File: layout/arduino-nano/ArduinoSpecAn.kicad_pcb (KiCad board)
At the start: 4 copper layers, 40.9 x 50.8 mm, 45 parts, among them J1 SMA, J2 SMA, P1 CONN_01X08, P2 CONN_01X06, P3 CONN_01X08, Q1 MMBT3904, Q2 MMBT3904, U1 AD8307, U2 AD9851, U3 LM7301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

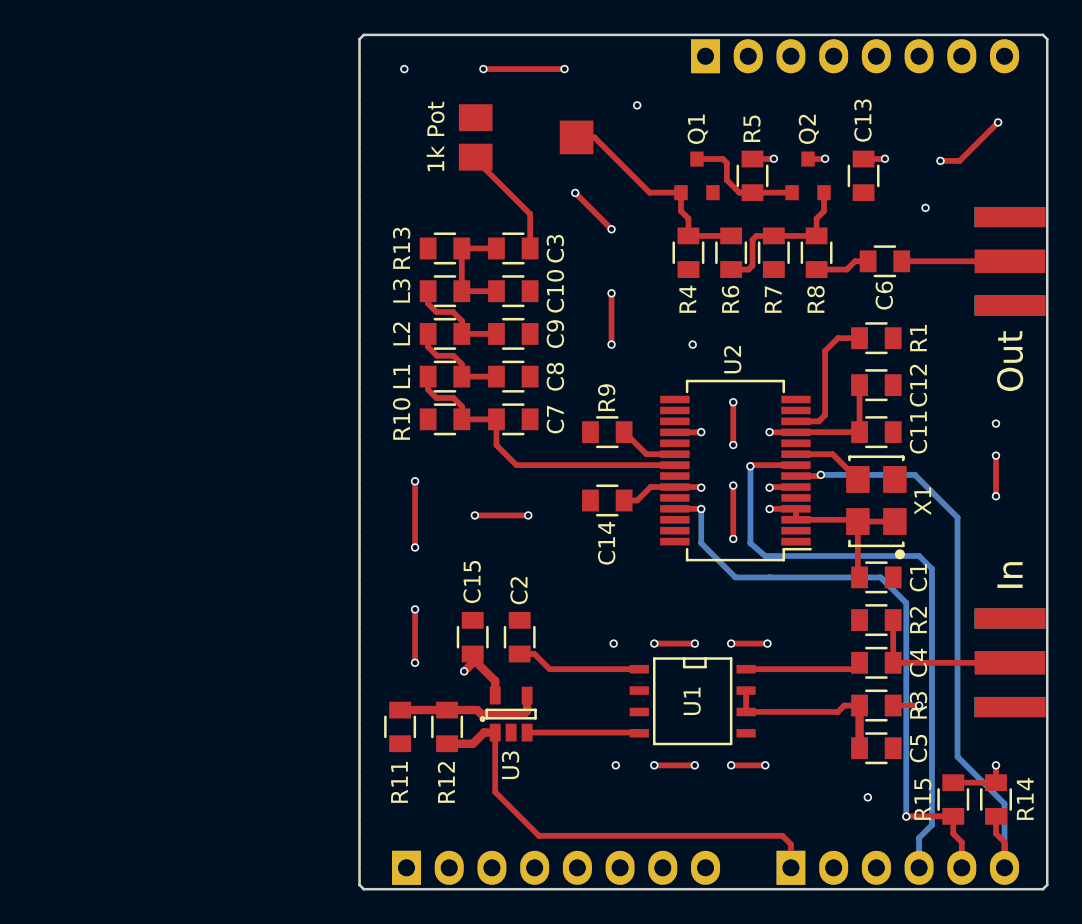
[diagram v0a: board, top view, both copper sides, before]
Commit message: Removed DDS
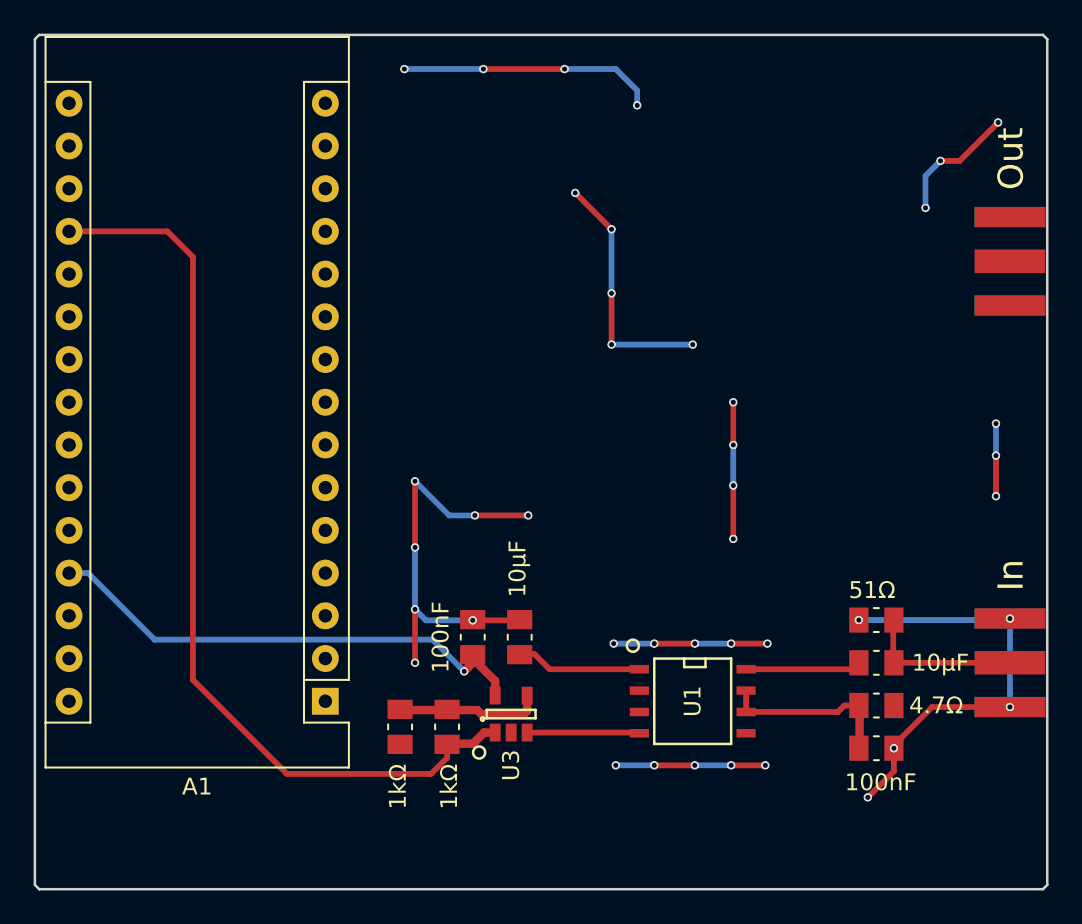
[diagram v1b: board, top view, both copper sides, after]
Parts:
- removed 1k Pot: POT, footprints:ST4ETB_Trim_Pot
- removed C1: .01uF, footprints:Custom_0805
- removed C10, C7: 10pF, footprints:Custom_0805
- removed C11, C12, C13, C14: .1uF, footprints:Custom_0805
- removed C3, C6: 10uF, footprints:Custom_0805
- removed C8, C9: 39pF, footprints:Custom_0805
- removed L1, L3: 270nH, footprints:Custom_0805
- removed L2: 470nH, footprints:Custom_0805
- removed P1, P3: CONN_01X08, Pin_Headers:Pin_Header_Straight_1x08
- removed P2: CONN_01X06, Pin_Headers:Pin_Header_Straight_1x06
- removed Q1, Q2: MMBT3904, footprints:SOT-23
- removed R1: 3k92, footprints:Custom_0805
- removed R10, R13, R4: 100, footprints:Custom_0805
- removed R14, R15: 2k, footprints:Custom_0805
- removed R5, R6, R7: 220, footprints:Custom_0805
- removed R8: 47, footprints:Custom_0805
- removed R9: 50, footprints:Custom_0805
- removed U2: AD9851, Housings_SSOP:SSOP-28_5.3x10.2mm_Pitch0.65mm
- removed X1: KC5032A, footprints:KC5032A-CM_SMD_Crystal
- added A1: Arduino_Nano_v3.x, Module:Arduino_Nano, F.Cu at (125.0, 125.5)
- C15, C5: value .1uF -> 100nF; footprint footprints:Custom_0805 -> Capacitor_SMD:C_0805_2012Metric_Pad1.15x1.50mm_HandSolder
- C2, C4: value 10uF -> 10µF; footprint footprints:Custom_0805 -> Capacitor_SMD:C_0805_2012Metric_Pad1.15x1.50mm_HandSolder
- R11, R12: value 1k -> 1kΩ; footprint footprints:Custom_0805 -> Resistor_SMD:R_0805_2012Metric_Pad1.15x1.50mm_HandSolder
- R2: value 51 -> 51Ω; footprint footprints:Custom_0805 -> Resistor_SMD:R_0805_2012Metric_Pad1.15x1.50mm_HandSolder
- R3: value 4R7 -> 4.7Ω; footprint footprints:Custom_0805 -> Resistor_SMD:R_0805_2012Metric_Pad1.15x1.50mm_HandSolder
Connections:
- net /5V renamed +5V
- J2 pad 1: Net-(C6-Pad2) -> (no net)
- U1 pad 3: Net-(U1-Pad3) -> (no net)
- U1 pad 5: Net-(U1-Pad5) -> (no net)
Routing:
- net /SLD: track 36.8 -> 0.00 mm, vias 1 -> 0
- net /A5: track 36.5 -> 0.00 mm, vias 1 -> 0
- net /A4: track 36.0 -> 0.00 mm, vias 2 -> 0
- net GND: track 86.4 -> 118.7 mm, vias 36 -> 41
- net /A0: track 26.9 -> 54.9 mm
- net Net-(C7-Pad1): track 18.7 -> 0.00 mm
- net Net-(1k1-Pad2): track 12.9 -> 0.00 mm
- net +5V: track 40.9 -> 30.2 mm, vias 11 -> 1
- net Net-(Q2-Pad2): track 9.56 -> 0.00 mm
- net Net-(R1-Pad1): track 8.06 -> 0.00 mm
- net Net-(Q1-Pad3): track 7.08 -> 0.00 mm
- net Net-(1k1-Pad1): track 6.77 -> 0.00 mm
- net /RF: track 6.67 -> 0.00 mm
- net Net-(C6-Pad2): track 6.43 -> 0.00 mm
- net Net-(C8-Pad1): track 6.02 -> 0.00 mm
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- removed copper zone on In2.Cu, net +5V
- removed copper zone on In1.Cu, net GND
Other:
- board size 40.9 x 50.8 mm -> 60.2 x 50.8 mm
